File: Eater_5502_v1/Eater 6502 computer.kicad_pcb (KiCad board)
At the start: 2 copper layers, 272.7 x 142.3 mm, 99 parts, among them J1 DE9_Plug, J2 PA_CONN, J3 PB_CONN, J4 ADDR_LOW, J5 DATA_CONN, J6 CPU_CONN, J7 CS_CONN, J8 PWR_IN, J9 ADDR_HIGH, SW1 RESET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

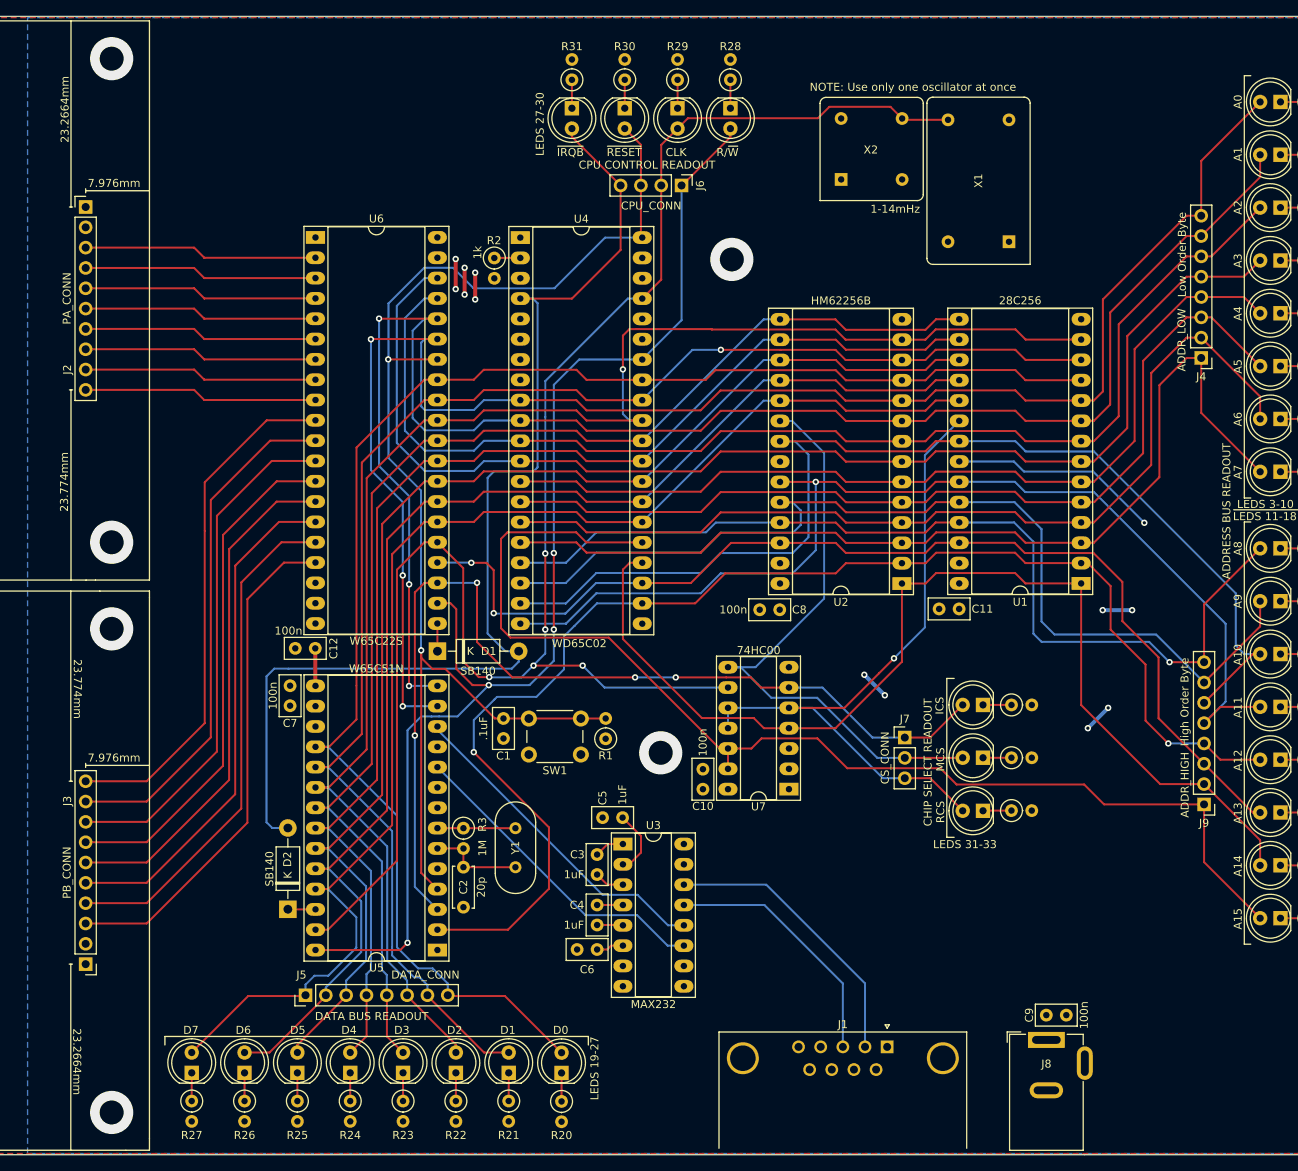
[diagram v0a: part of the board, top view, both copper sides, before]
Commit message: updated board design to include bigger capacitor footprints, added the bulk decoupling cap to the power input, and made text larger in places to improve readability
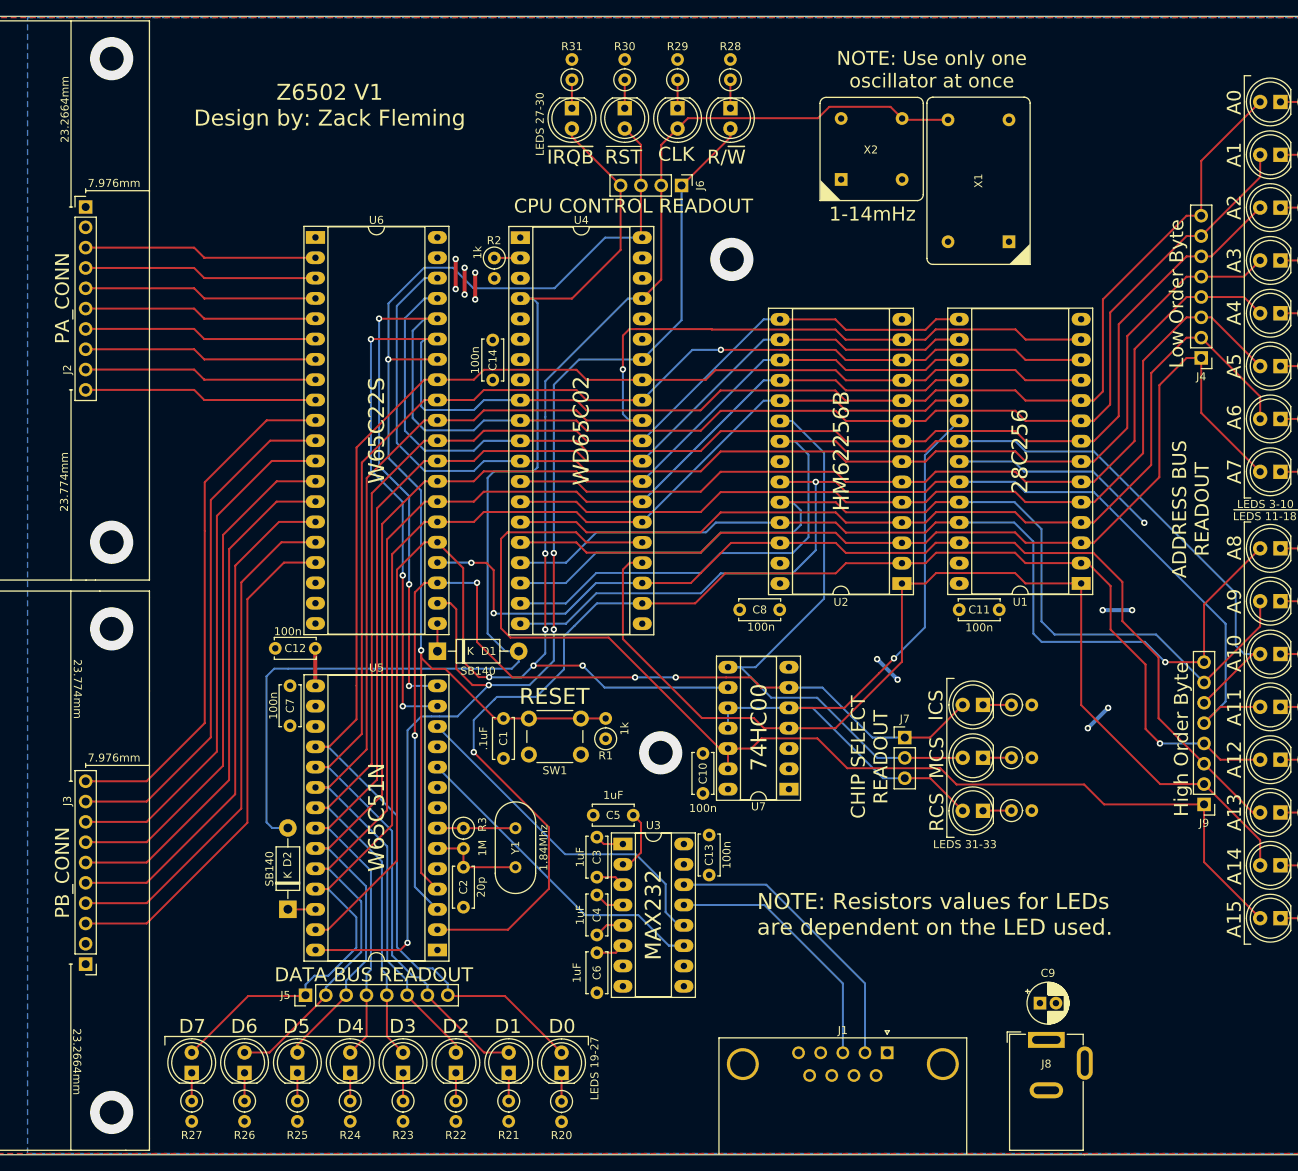
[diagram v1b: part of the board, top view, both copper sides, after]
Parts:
- added C13: 100n, Capacitor_THT:C_Disc_D5.0mm_W2.5mm_P5.00mm, F.Cu at (202.0, 114.5)
- added C14: 100n, Capacitor_THT:C_Disc_D5.0mm_W2.5mm_P5.00mm, F.Cu at (175.0, 57.6)
- C1, C10, C11, C12, C3, C4, C5, C6, C7, C8: footprint Capacitor_THT:C_Disc_D5.0mm_W2.5mm_P2.50mm -> Capacitor_THT:C_Disc_D5.0mm_W2.5mm_P5.00mm
- C9: value 100n -> 100uF; footprint Capacitor_THT:C_Disc_D5.0mm_W2.5mm_P2.50mm -> Capacitor_THT:CP_Radial_D5.0mm_P2.00mm
- moved C9 1.70 mm to (243.4, 135.5)
- moved C5 1.37 mm to (192.6, 112.0)
- moved C4 1.24 mm to (188.0, 127.0)
- moved J1 0.74 mm to (224.3, 141.7)
- moved C10 0.53 mm to (201.3, 109.3)
- moved C6 0.41 mm to (188.0, 129.2), turned to -90 degrees
- moved C3 0.33 mm to (188.0, 119.7)
- moved C11 0.10 mm to (233.3, 86.3), turned to 0 degrees
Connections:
- J1 pad 0: (no net) -> GND
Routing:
- net Net-(U3-R1O): track 41.3 -> 43.6 mm
- net Net-(U3-T10): track 35.7 -> 36.4 mm
- net Net-(U3-R1I): track 31.9 -> 32.6 mm
- net /a12: track 168.4 -> 169.0 mm
- net Net-(U3-C2-): track 3.24 -> 3.83 mm
- net Net-(U3-C2+): track 3.23 -> 3.77 mm
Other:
- board text added: "Board Design notes: Mounting Via Positions in mm (from corner with triangle): -#: ( x , y ) -1 : ( 5.2832, 5.2832) -2 : (115.2144, 5.2832) -3 : (267.9700, 4.2744) -4 : (192.7352, 30.3784) -5 : ( 5.2832, 56.7252) -6 : (115.2144, 65.7352) -7 : ( 5.2832, 76.5556) -8 : (115.2144, 76.5556) -9 : (183.8452, 92.0496) -10: ( 5.2832, 137.0076) -11: (115.2144, 137.0076) -12: (267.9700, 137.5664) All mountin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"
- board text added: "NOTE: Resistors values for LEDs are dependent on the LED used."
- board text added: "Z6502 V1 Design by: Zack Fleming"
- board text added: "~{RST}"
- board text removed: "Board Design notes: Mounting Via Positions in mm (from corner with triangle): (x, y) -1 : ( 5.2832, 5.2832) -2 : (115.2144, 5.2832) -3 : (267.9700, 4.2744) -4 : (192.7352, 30.3784) -5 : ( 5.2832, 56.7252) -6 : (115.2144, 65.7352) -7 : ( 5.2832, 76.5556) -8 : (115.2144, 76.5556) -9 : (183.8452, 92.0496) -10: ( 5.2832, 137.0076) -11: (115.2144, 137.0076) -12: (267.9700, 137.5664) All mounting vias 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"
- board text removed: "~{RESET}"
